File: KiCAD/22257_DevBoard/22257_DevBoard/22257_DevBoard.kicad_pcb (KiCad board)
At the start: 6 copper layers, 213.1 x 99.1 mm, 92 parts, among them J1 TD-120-G-AACON40_2X20_TU_HTS_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, J2 TD-120-G-AACON40_2X20_TU_HTS_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, J3 Screw_Terminal_01x02, J4 Conn_Coaxial, J5 Conn_Coaxial, J6 Conn_Coaxial, J7 Conn_Coaxial, U10 74LVC1G17, U11 74LVC1G17, U3 TPS73633DBV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

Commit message: DONE ROUTINGgit add .git add .
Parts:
- added C25: 47u, Capacitor_SMD:C_0603_1608Metric, F.Cu at (34.7, 42.9)
- moved TP12 23.0 mm to (117.4, 83.2)
- moved TP16 5.36 mm to (170.2, 7.65)
- moved TP15 4.93 mm to (169.9, 11.6)
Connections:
- J1 pad 9: /MicroZed_Headers/35_L15 -> BRD_10MHz_IN
- JX1 pad 84: /MicroZed_Headers/35_L15 -> BRD_10MHz_IN
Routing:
- net GND: track 0.00 -> 155.0 mm, vias 0 -> 285
- net BRD_10MHz_IN: track 0.00 -> 154.6 mm, vias 0 -> 1
- net /MicroZed_Headers/35_L15: track 11.3 -> 0.00 mm
- net Net-(U4-SW): track 1.11 -> 11.2 mm, vias 0 -> 2
- net +3.3V: track 95.2 -> 102.4 mm, vias 42 -> 46
- net Net-(U5-A1): track 0.00 -> 6.39 mm
- net Net-(U5-A0): track 0.00 -> 5.50 mm
- net BRD_10MHz_OUT: track 181.1 -> 178.7 mm
- net Net-(D4-A): track 0.00 -> 2.26 mm
- net Net-(D5-A): track 0.00 -> 2.23 mm
- net Net-(D3-A): track 0.00 -> 2.23 mm
- net Net-(D6-A): track 0.00 -> 2.22 mm
- net /MicroZed_Headers/35_J14: track 22.2 -> 23.0 mm
- net TCXO_OE: track 109.9 -> 110.6 mm
- net Net-(U4-VFB): track 4.59 -> 5.17 mm
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
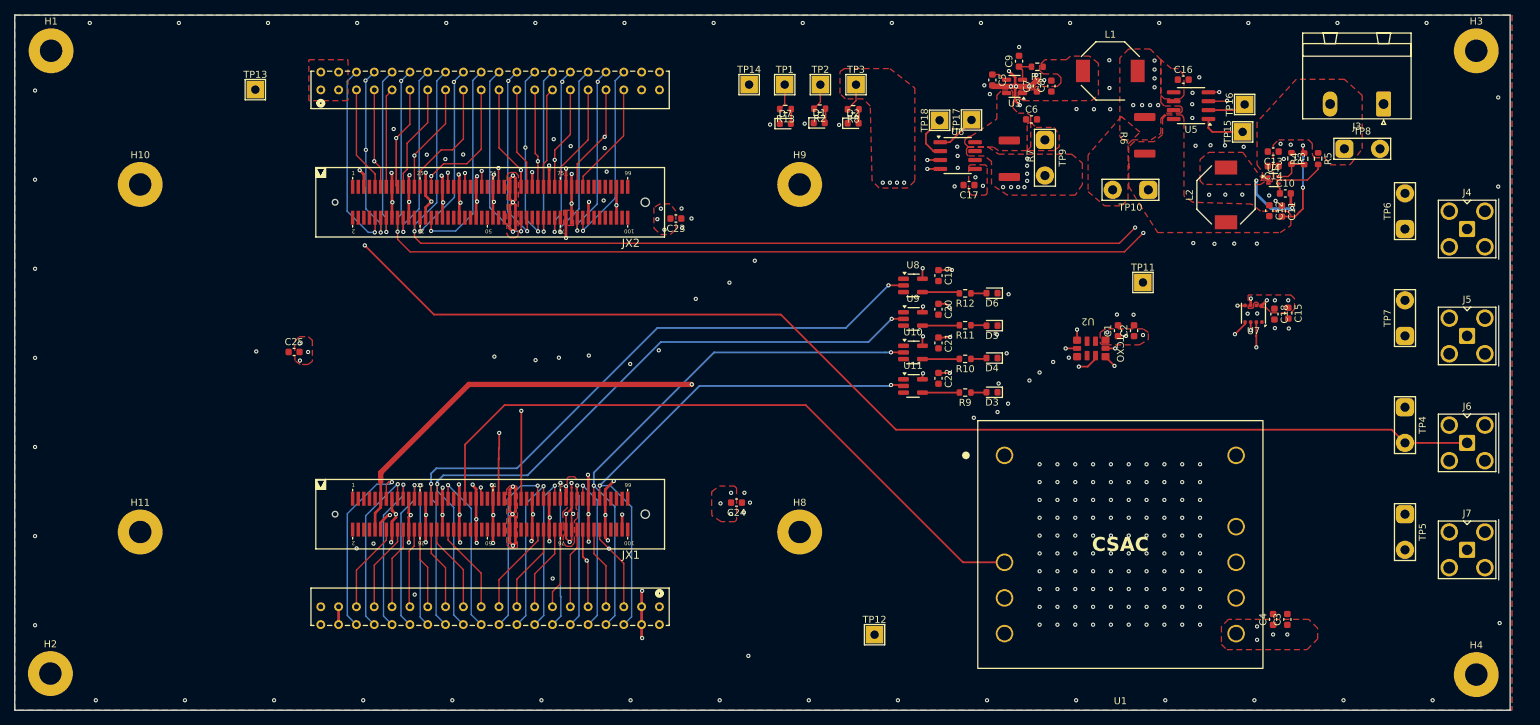
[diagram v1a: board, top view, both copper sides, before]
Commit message: Done with routing-related DRCs!!
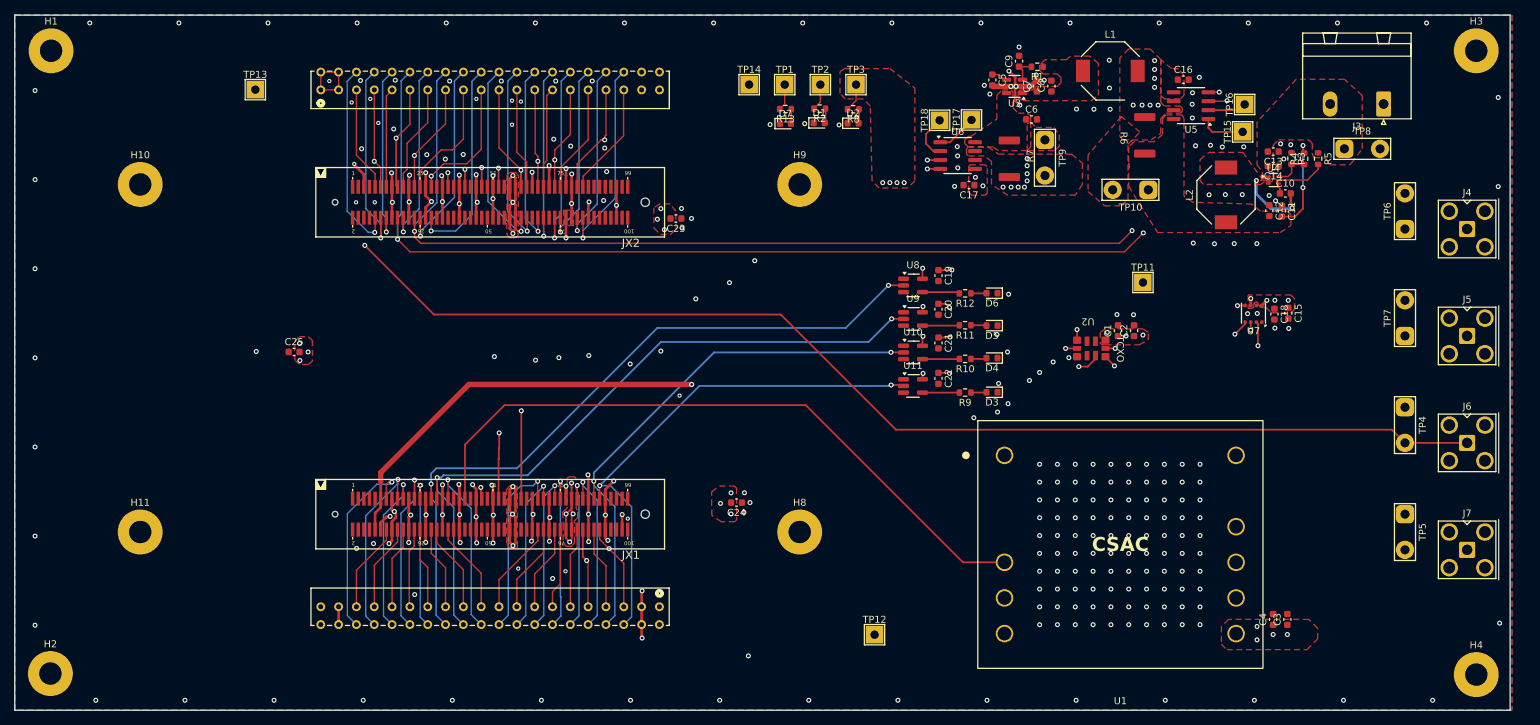
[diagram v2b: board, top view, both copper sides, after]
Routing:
- net +5V: track 54.0 -> 67.7 mm
- net /MicroZed_Headers/34_T12: track 26.4 -> 28.7 mm
- net /MicroZed_Headers/34_P16: track 26.9 -> 28.9 mm
- net CSAC_Rx: track 111.8 -> 113.9 mm
- net /MicroZed_Headers/34_W18: track 25.7 -> 27.5 mm
- net /MicroZed_Headers/34_R14: track 27.2 -> 28.6 mm
- net /MicroZed_Headers/34_R18: track 25.3 -> 26.6 mm
- net TST_02: track 100.1 -> 101.3 mm
- net PM_SDA_5V: track 161.2 -> 162.3 mm
- net ES_SCK: track 136.6 -> 137.7 mm
- net CSAC_Tune: track 116.6 -> 117.6 mm
- net /MicroZed_Headers/35_N16: track 23.0 -> 24.1 mm
- net ES_SDO: track 134.0 -> 135.0 mm
- net CSAC_PPS_IN: track 159.7 -> 160.5 mm
- net CSAC_Tx: track 100.6 -> 101.3 mm
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
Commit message: Almost done silkscreening :,)
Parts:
- moved J4 1.63 mm to (203.5, 25.5)
- moved J5 1.63 mm to (203.5, 40.7)
- moved J6 1.63 mm to (203.5, 55.9)
- moved J7 1.63 mm to (203.5, 71.2)
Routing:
- net BRD_PPS_OUT: track 159.3 -> 161.0 mm
- net BRD_10MHz_OUT: track 178.7 -> 180.4 mm
- net BRD_PPS_IN: track 195.5 -> 197.1 mm
- net BRD_10MHz_IN: track 154.6 -> 156.3 mm
- net +3.3V: track 102.3 -> 102.9 mm
- net GND: vias 299 -> 295
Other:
- board text added: "10 MHz IN"
- board text added: "10MHz OUT"
- board text added: "PPS IN"
- board text added: "PPS OUT"

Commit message: Done :D
Existence is pain
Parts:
- R6, R7: value R_Shunt_US -> 2m
- moved C6 0.42 mm to (139.6, 9.40)
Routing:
- net GND: vias 295 -> 296
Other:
- board text added: "+"
- board text added: "-"
- board text added: "12V"
- board text added: "3V3"
- board text added: "5V"
- board text added: "GND"
- board text added: "Ian Dolfi Drew Schacke Tanner Smith Luke Schrom Eva Czukkermann Nsadhu Muyinda"
- board text added: "RIT MSD 22257 Precision Time Card Development Board"
- board text added: "TST 1"
- board text added: "TST 2"
- board text added: "TST 3"
- board text added: "TST 4"
